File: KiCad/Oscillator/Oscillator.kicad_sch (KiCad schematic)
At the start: 40 parts, among them J1 Screw_Terminal_01x02, J2 Screw_Terminal_01x03, Q1 NPN, Q2 PNP, Q3 NPN, Q4 PNP, U1 40106, U2 TL074

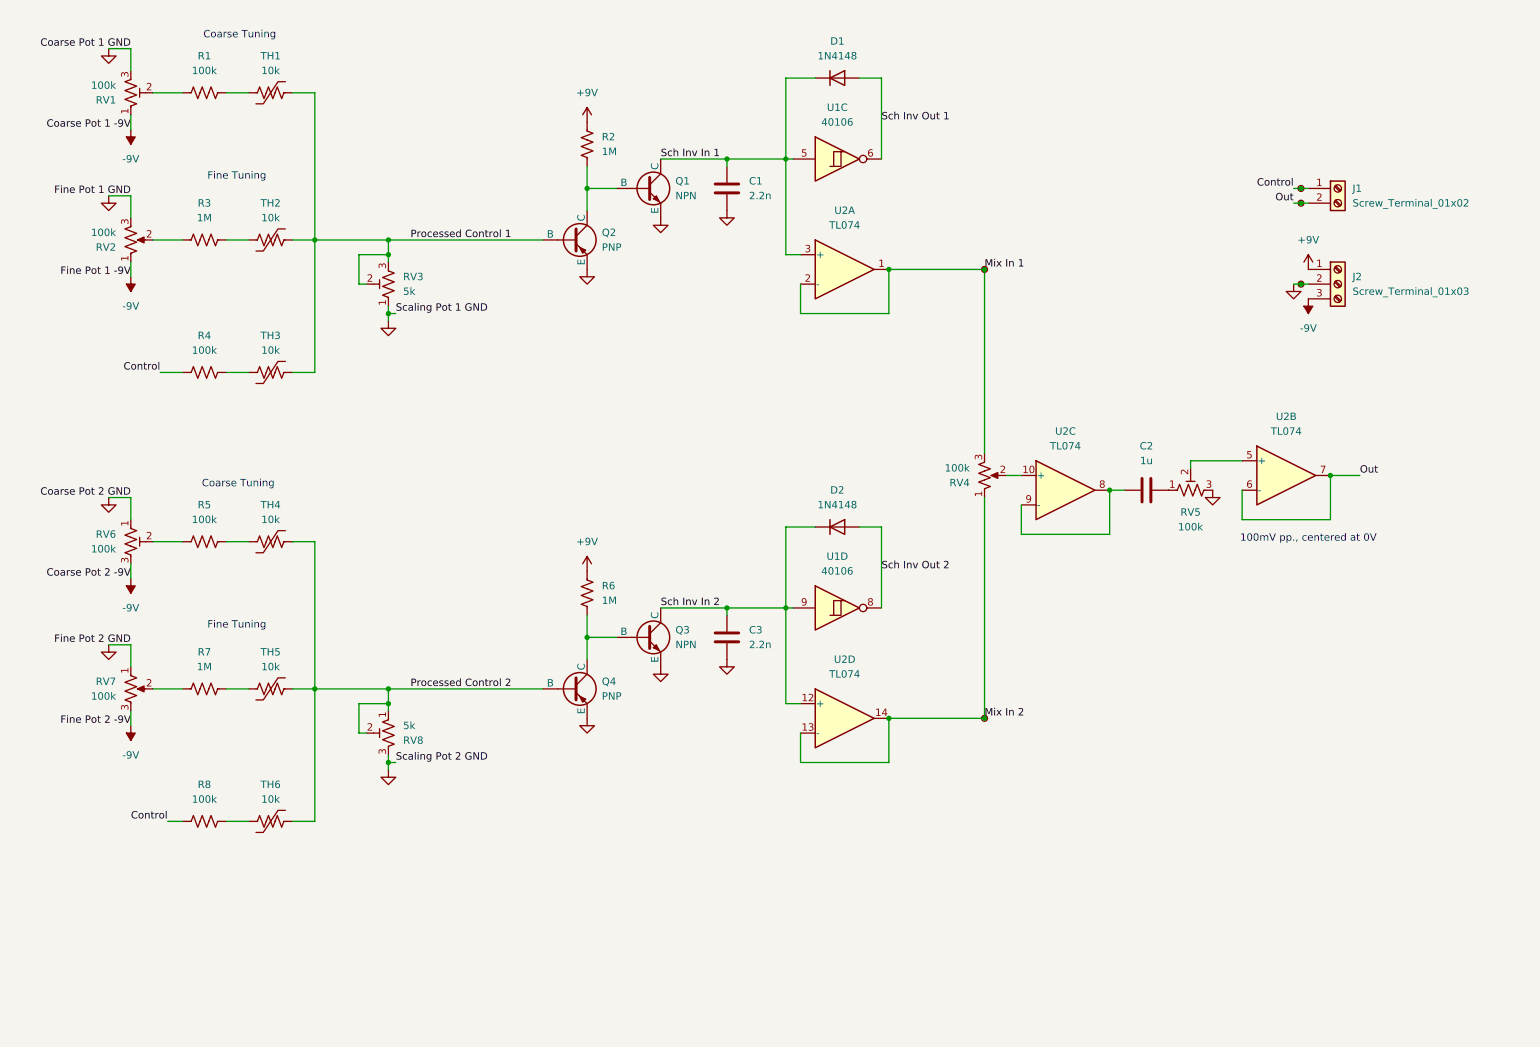
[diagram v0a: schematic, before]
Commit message: power pcb layout done
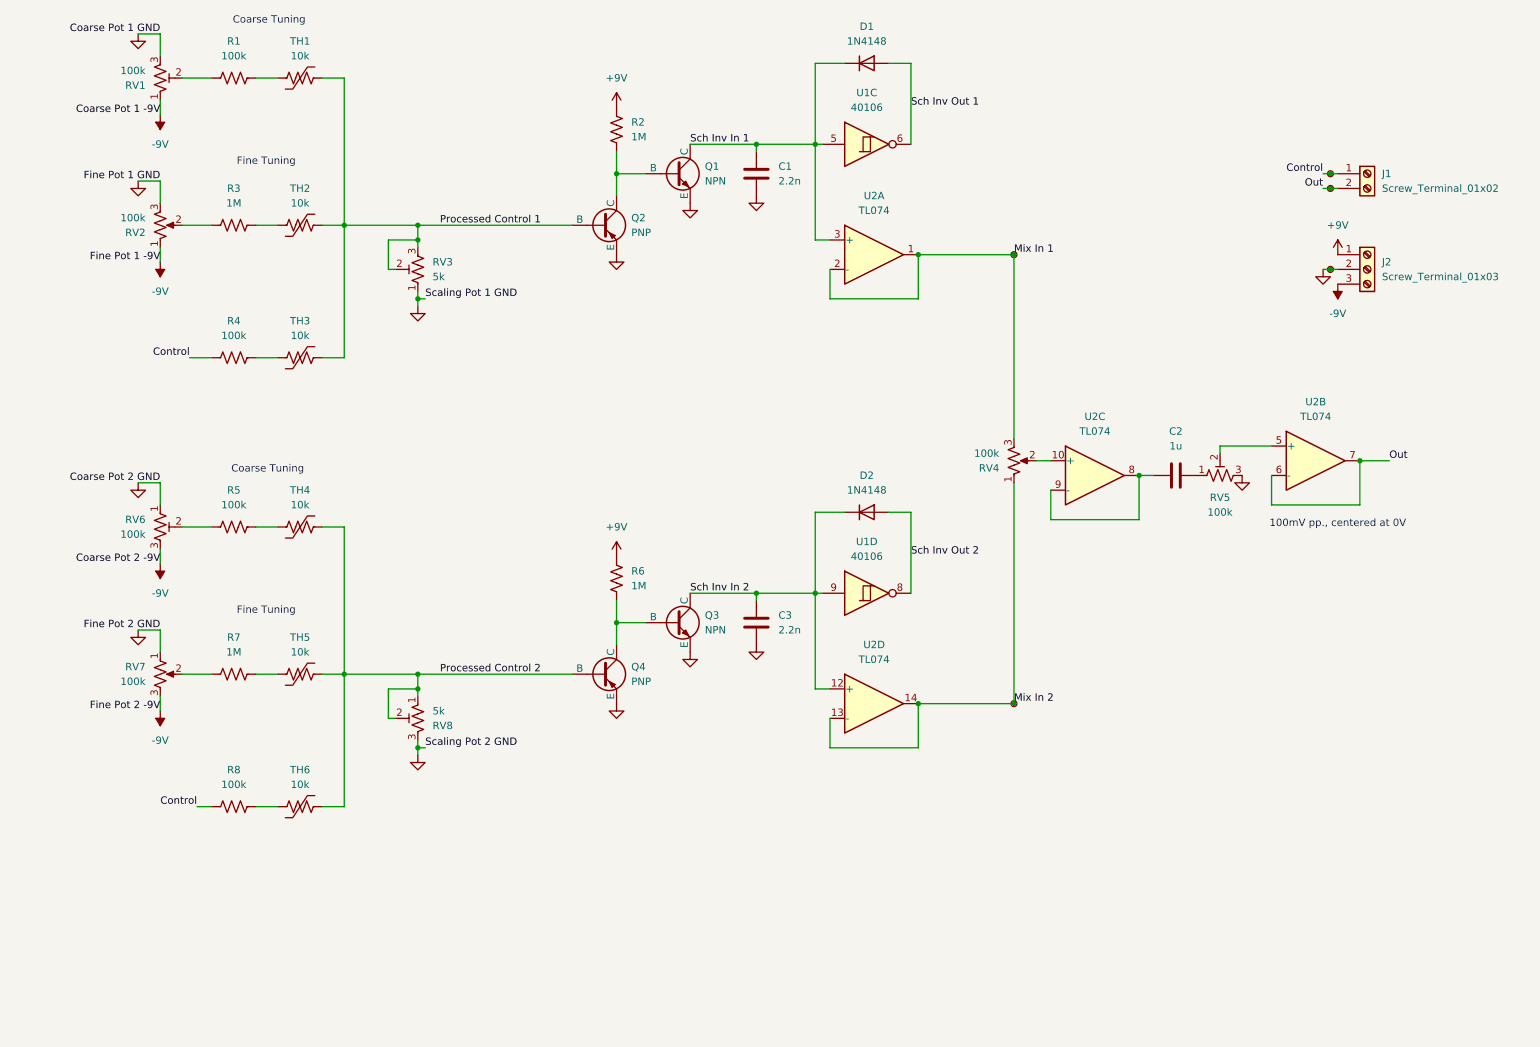
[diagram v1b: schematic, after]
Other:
- moved on the sheet: C1, C2, C3, D1, D2, J1, J2, Q1, Q2, Q3, Q4, R1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

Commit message: added mounting holes to schematics, adjusted board sizes
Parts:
- added H1, H2, H3, H4: MountingHole, MountingHole:MountingHole_3.2mm_M3, symbol Mechanical:MountingHole

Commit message: preparation to merge project back into one board
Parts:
- C1, C2, C3: KiLib_Generator (none) -> capacitor/THT/other
- D1, D2: KiLib_Generator (none) -> diode/THT
- R1, R2, R3, R4, R5, R6, R7, R8: KiLib_Generator (none) -> SMD_2terminal_chip_molded
- RV2, RV4, RV7: KiLib_Generator (none) -> potentiometer/THT
- TH1, TH2, TH3, TH4, TH5, TH6: KiLib_Generator (none) -> resistor/THT
- U1, U2: KiLib_Generator (none) -> package/DIP/legacy
- renumbered TP10 to TP1, TP20 to TP2, TP4 to TP3, TP6 to TP4, TP11 to TP5
